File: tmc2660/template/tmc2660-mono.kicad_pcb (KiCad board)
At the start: 4 copper layers, 25 x 40 mm, 18 parts, among them J100 0R, M100 Mount, M101 Mount, P100 Motor, U100 TMC2660

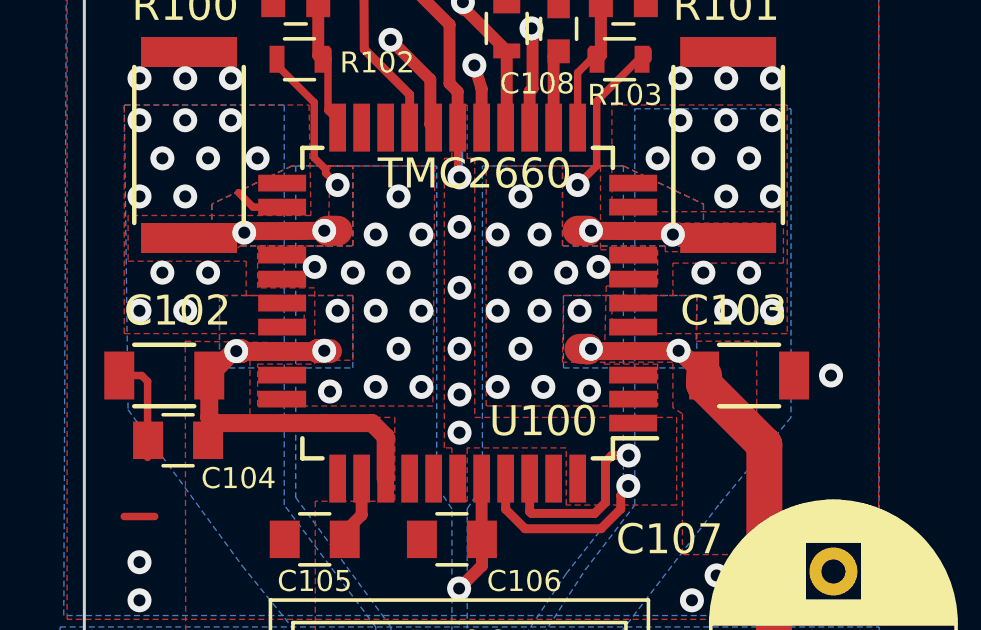
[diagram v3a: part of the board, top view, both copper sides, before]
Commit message: Add signal description also on front silk-screen.
o In template: move a designator out of the way to not collide with that
  description.
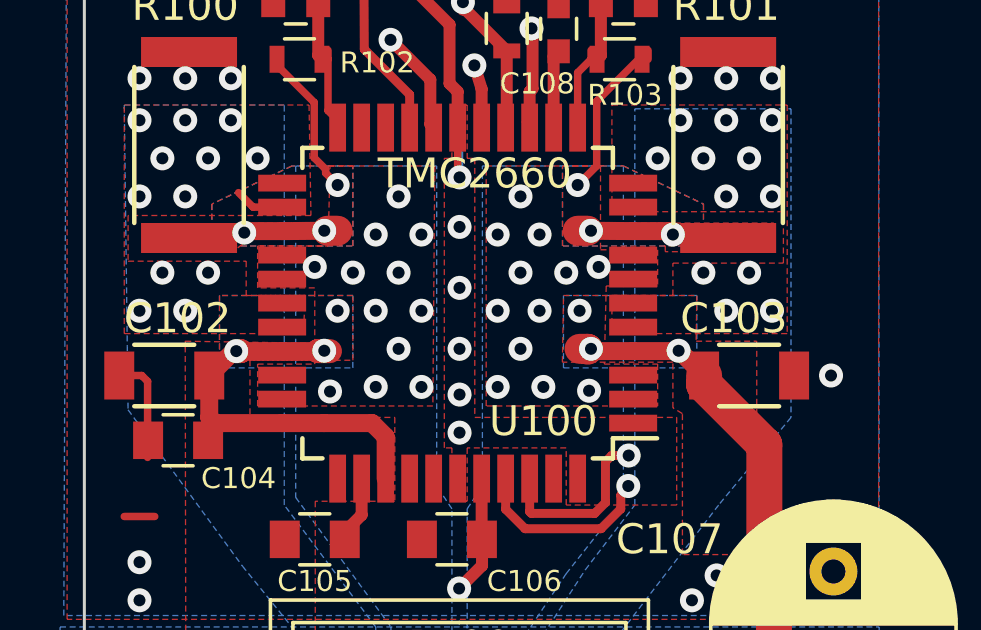
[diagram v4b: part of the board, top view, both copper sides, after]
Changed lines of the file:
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@@
     (tags "capacitor 1206")
     (attr smd)
-    (fp_text reference C102 (at -0.4445 2.159) (layer F.SilkS)
+    (fp_text reference C102 (at -0.4445 1.905) (layer F.SilkS)
       (effects (font (size 1 1) (thickness 0.15)))
     )
@@
     (tags "capacitor 1206")
     (attr smd)
-    (fp_text reference C103 (at -0.508 -2.159) (layer F.SilkS)
+    (fp_text reference C103 (at -0.508 -1.905) (layer F.SilkS)
       (effects (font (size 1 1) (thickness 0.15)))
     )
